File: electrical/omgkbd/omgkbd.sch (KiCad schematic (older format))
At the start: 0 parts

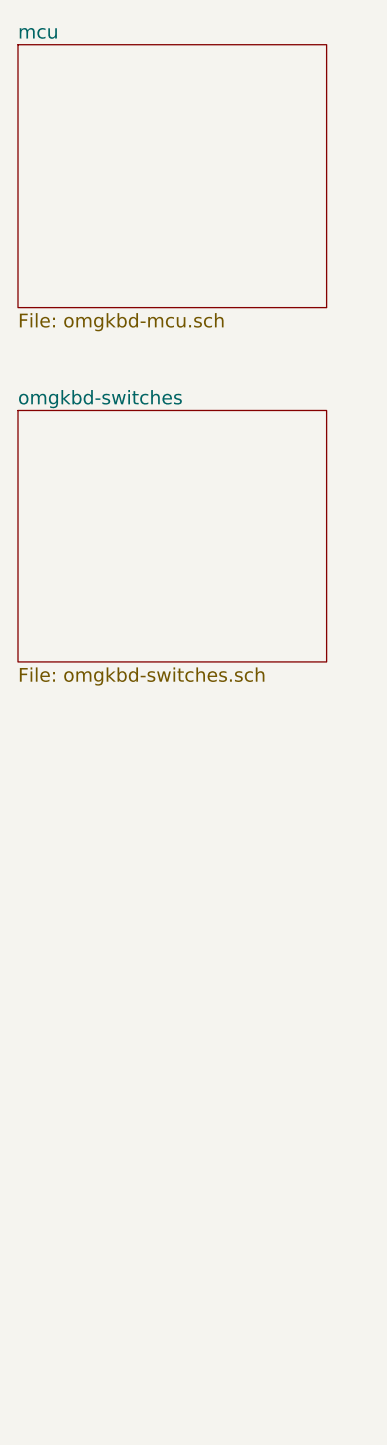
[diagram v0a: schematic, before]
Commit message: Added switches, back and ambient light schematics
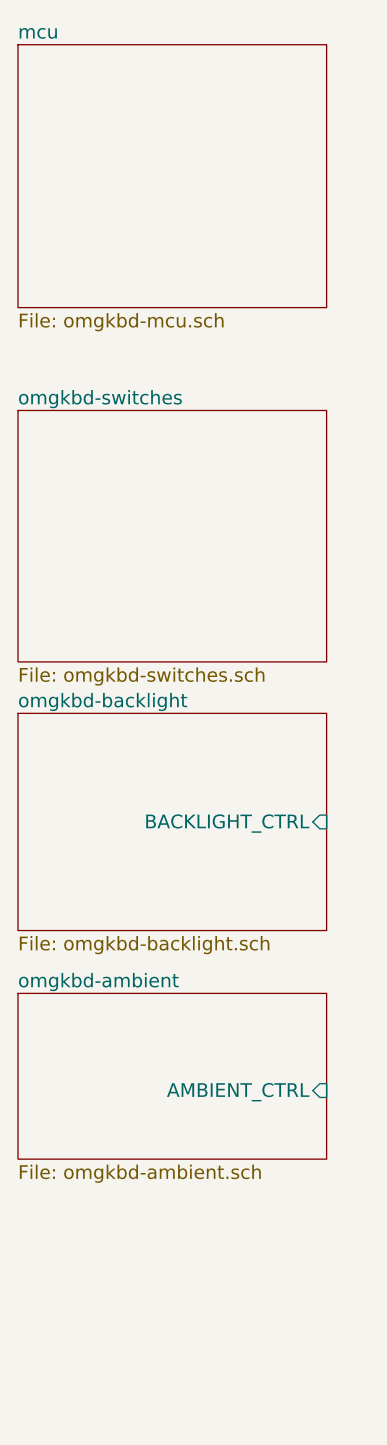
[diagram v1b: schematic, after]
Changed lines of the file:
@@
 $Descr A3 16535 11693
 encoding utf-8
-Sheet 1 3
+Sheet 1 5
 Title "Jellyfish"
 Date "2017-10-29"
@@
 F1 "omgkbd-switches.sch" 60
 $EndSheet
+$Sheet
+S 800  3775 1350 950
+U 59FEE73D
+F0 "omgkbd-backlight" 60
+F1 "omgkbd-backlight.sch" 60
+F2 "BACKLIGHT_CTRL" I R 2150 4250 60
+$EndSheet
+$Sheet
+S 800  5000 1350 725
+U 59FEE9F5
+F0 "omgkbd-ambient" 60
+F1 "omgkbd-ambient.sch" 60
+F2 "AMBIENT_CTRL" I R 2150 5425 60
+$EndSheet
 $EndSCHEMATC

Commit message: Started working on connector and power
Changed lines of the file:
@@
 $Descr A3 16535 11693
 encoding utf-8
-Sheet 1 5
+Sheet 1 6
 Title "Jellyfish"
 Date "2017-10-29"
@@
 F0 "omgkbd-switches" 60
 F1 "omgkbd-switches.sch" 60
+F2 "SWITCHES" O R 2150 2950 60
 $EndSheet
 $Sheet
@@
 F2 "AMBIENT_CTRL" I R 2150 5425 60
 $EndSheet
+$Sheet
+S 800  6025 1375 750
+U 5A035936
+F0 "omgkbd-pwr" 60
+F1 "omgkbd-pwr.sch" 60
+$EndSheet
 $EndSCHEMATC
